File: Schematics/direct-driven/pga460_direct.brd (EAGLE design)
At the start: 20 parts, among them IC1 PGA460TPWQ1, T1 B78416A2232A003

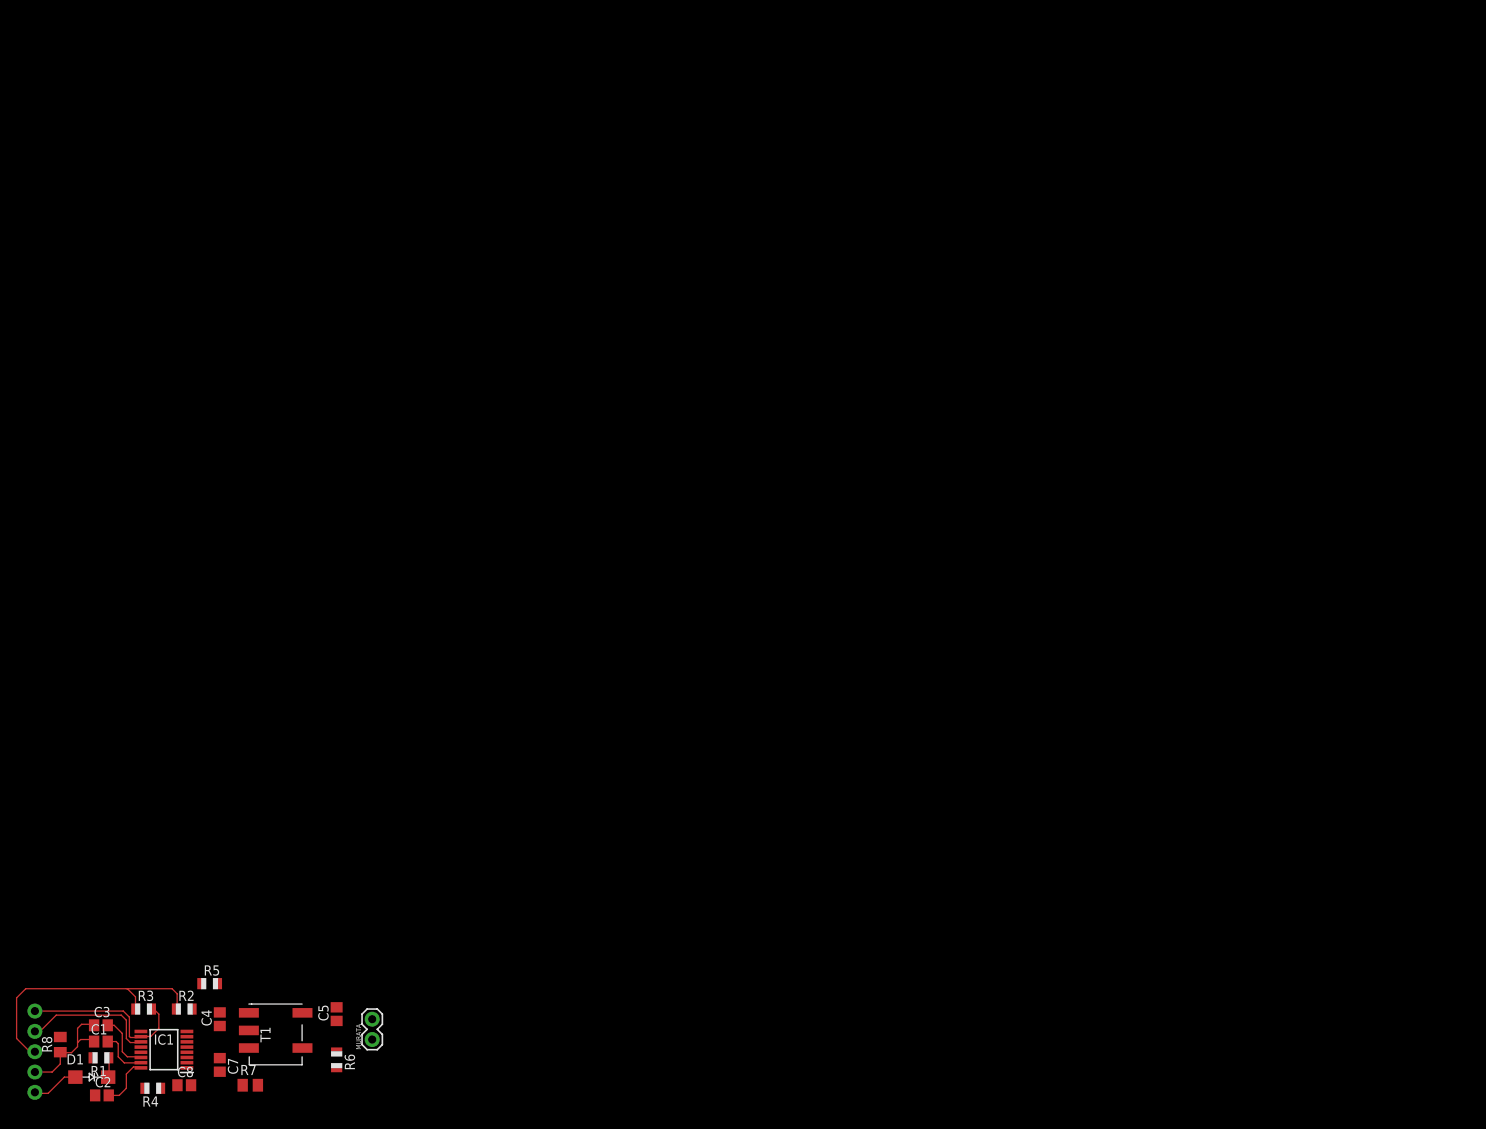
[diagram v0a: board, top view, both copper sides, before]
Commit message: update report. add in mega shield template.
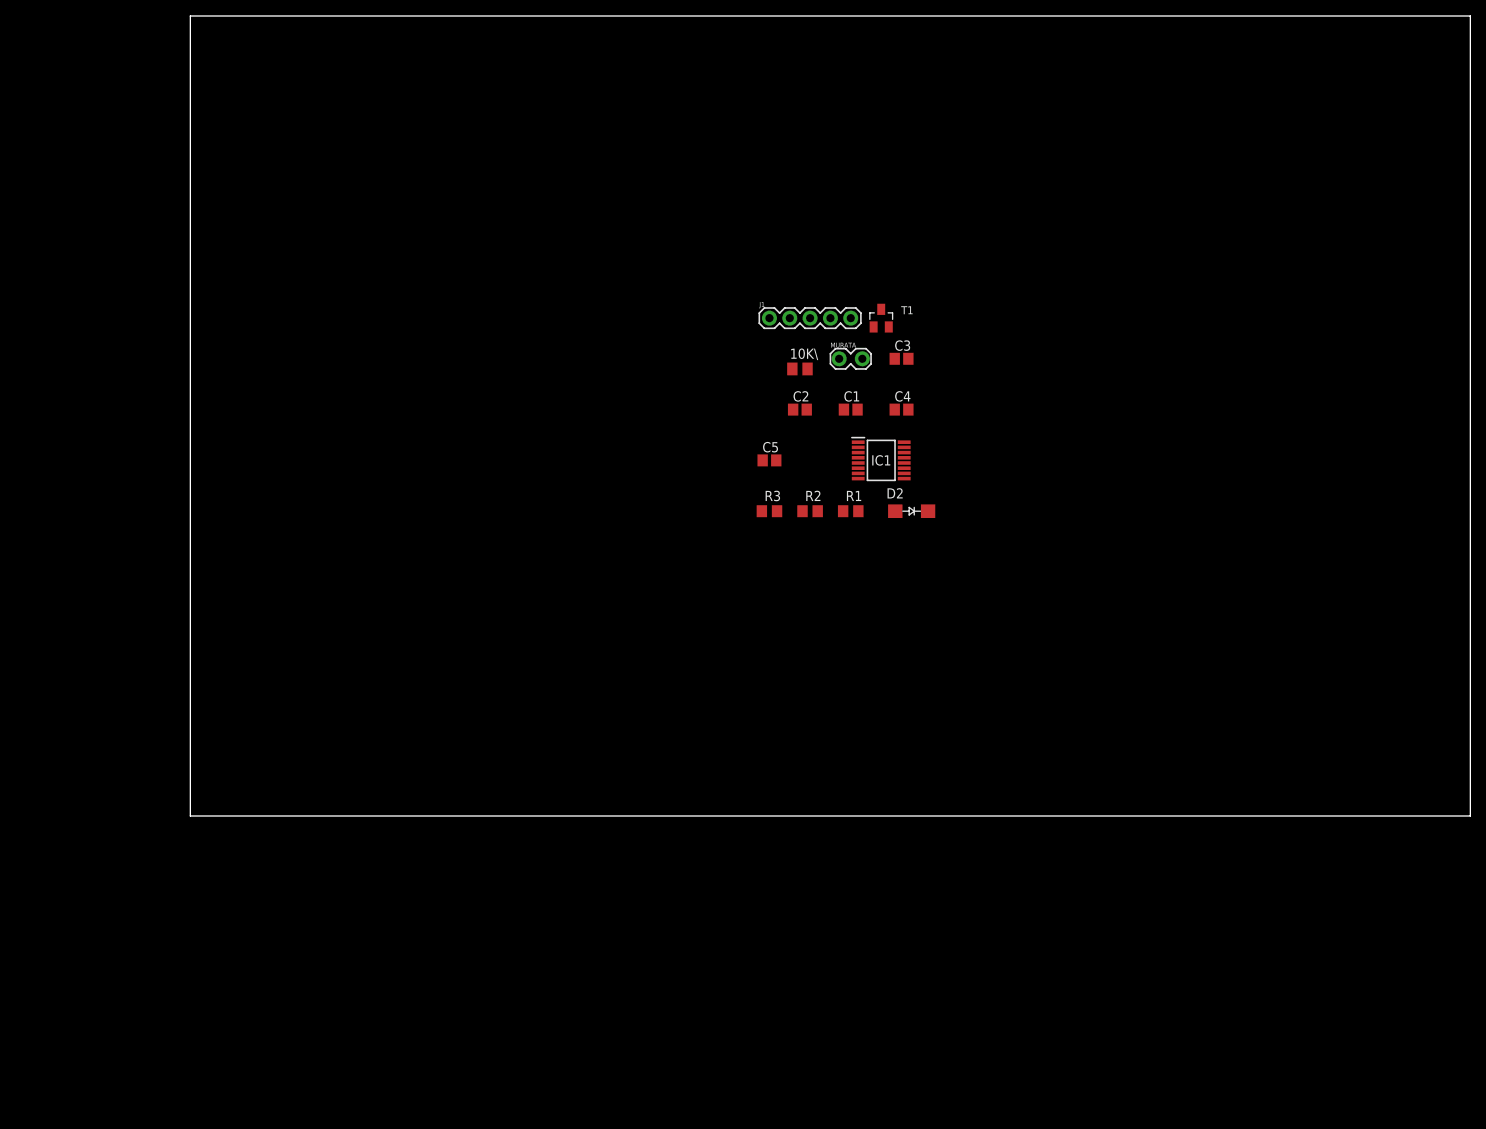
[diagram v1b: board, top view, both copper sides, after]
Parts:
- removed C7: 390pF, adafruit:C0805
- removed C8: 0.033uF, adafruit:C0805
- removed D1: 1N4007, casovac:SMA
- removed R4: 10k, adafruit:R0805
- removed R5: 100, adafruit:R0805
- removed R6: 2.7k, adafruit:R0805
- removed R7: 3K, rcl:M0805
- removed R8: 0, adafruit:M0805
- added 10K\: (no value), rcl:M0805
- added D2: 1N4007, casovac:SMA
- C2: value 0.1 uF -> 0.1uF
- C4: value 100uF -> 390pF
- C5: value 680pF -> 0.033uF
- MURATA: value ma59mf14-7n -> ma58mf14-7n; device SparkFun-Connectors:1X02 -> SparkFun-Connectors:1X02_LOCK
- R1: value 10 -> 10k; device adafruit:R0805 -> rcl:R0805
- R2, R3: device adafruit:R0805 -> rcl:R0805
- T1: value B78416A2232A003 -> BSS84; device SamacSys_Parts:B78416A2232A003 -> nxp_60_1_1:SOT23
- moved C3 130.2 mm to (88.9, 57.1)
- moved J1 126.2 mm to (72.4, 62.2), flipped to the top, turned to 0 degrees
- moved C1 122.6 mm to (82.5, 50.8)
- moved C2 122.3 mm to (76.2, 50.8)
- moved T1 117.2 mm to (86.4, 62.2), turned to 0 degrees
- moved IC1 116.0 mm to (86.4, 44.5), turned to 0 degrees
- moved R1 116.0 mm to (82.5, 38.1), turned to 0 degrees
- moved C4 114.3 mm to (88.9, 50.8), turned to 0 degrees
- moved MURATA 103.3 mm to (81.3, 57.1), turned to 0 degrees
- moved R2 100.0 mm to (77.5, 38.1)
- moved R3 100.0 mm to (72.4, 38.1)
- moved C5 87.9 mm to (72.4, 44.5), turned to 0 degrees
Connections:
- removed net N$10: C7.2, R7.1
- removed net N$5: IC1.12, R4.2
- removed net N$6: IC1.9, R2.2
- removed net N$8: C5.2, MURATA.1, R6.1, R7.2, T1.4
- new net N$7: C2.1, IC1.14
- net 5V: now also R2.2, R3.2; no longer R2.1, R3.1
- net GND: now also 10K\.1, C1.2, C2.2, C3.2, R1.2; no longer C1.1, C2.1, C3.1, C4.1, C8.2, R4.1, R6.2, R8.1, R8.2, T1.6
- net INN: now also C5.2; no longer C8.1
- net INP: now also C4.2; no longer C7.1
- net N$1: now also IC1.12, R1.1; no longer C1.2, IC1.15, R1.2
- net N$2: now also C1.1, D2.K, IC1.15; no longer C3.2, IC1.14
- net N$3: now also C3.1; no longer C2.2
- net N$4: now also IC1.9, R3.1; no longer D1.K, R1.1
- net OUTA: now also 10K\.2, C4.1, MURATA.1, T1.3; no longer T1.1
- net OUTB: now also T1.1; no longer T1.3
- net RXD: now also J1.1; no longer J1.2
- net TXD: now also J1.2, R2.1; no longer J1.1, R3.2
- net VPWR: now also D2.A; no longer C4.2, D1.A, R5.1, R5.2
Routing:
- net N$16: track 33.1 -> 0.00 mm
- net N$14: track 16.2 -> 0.00 mm
- net N$18: track 15.0 -> 0.00 mm
- net N$15: track 8.81 -> 0.00 mm
- net N$9: track 6.78 -> 0.00 mm
- net N$7: track 6.32 -> 0.00 mm
- net N$11: track 6.01 -> 0.00 mm
- net N$12: track 5.03 -> 0.00 mm
- net N$17: track 4.75 -> 0.00 mm
- net N$19: track 4.23 -> 0.00 mm
- net N$13: track 2.34 -> 0.00 mm
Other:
- board outline added: 160 x 100 mm
